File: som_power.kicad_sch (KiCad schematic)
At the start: 94 parts, among them J1 Hermaphroditic_Molex_203456-0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, Q10 DMG1012T-7, Q11 DMG1012T-7, Q17 DMG1012T-7, Q18 DMG1012T-7, Q20 DMG1012T-7, Q22 DMG1012T-7, Q37 DMG1012T-7, Q38 DMG1012T-7, Q7 DMG1012T-7, Q8 DMG1012T-7, SW2 SW_SPDT_PCM12SMTR, U70 MAX16150A_SOT, U72 TPS3840PL30DBVR, U74 SN74LVC2G07DCKR

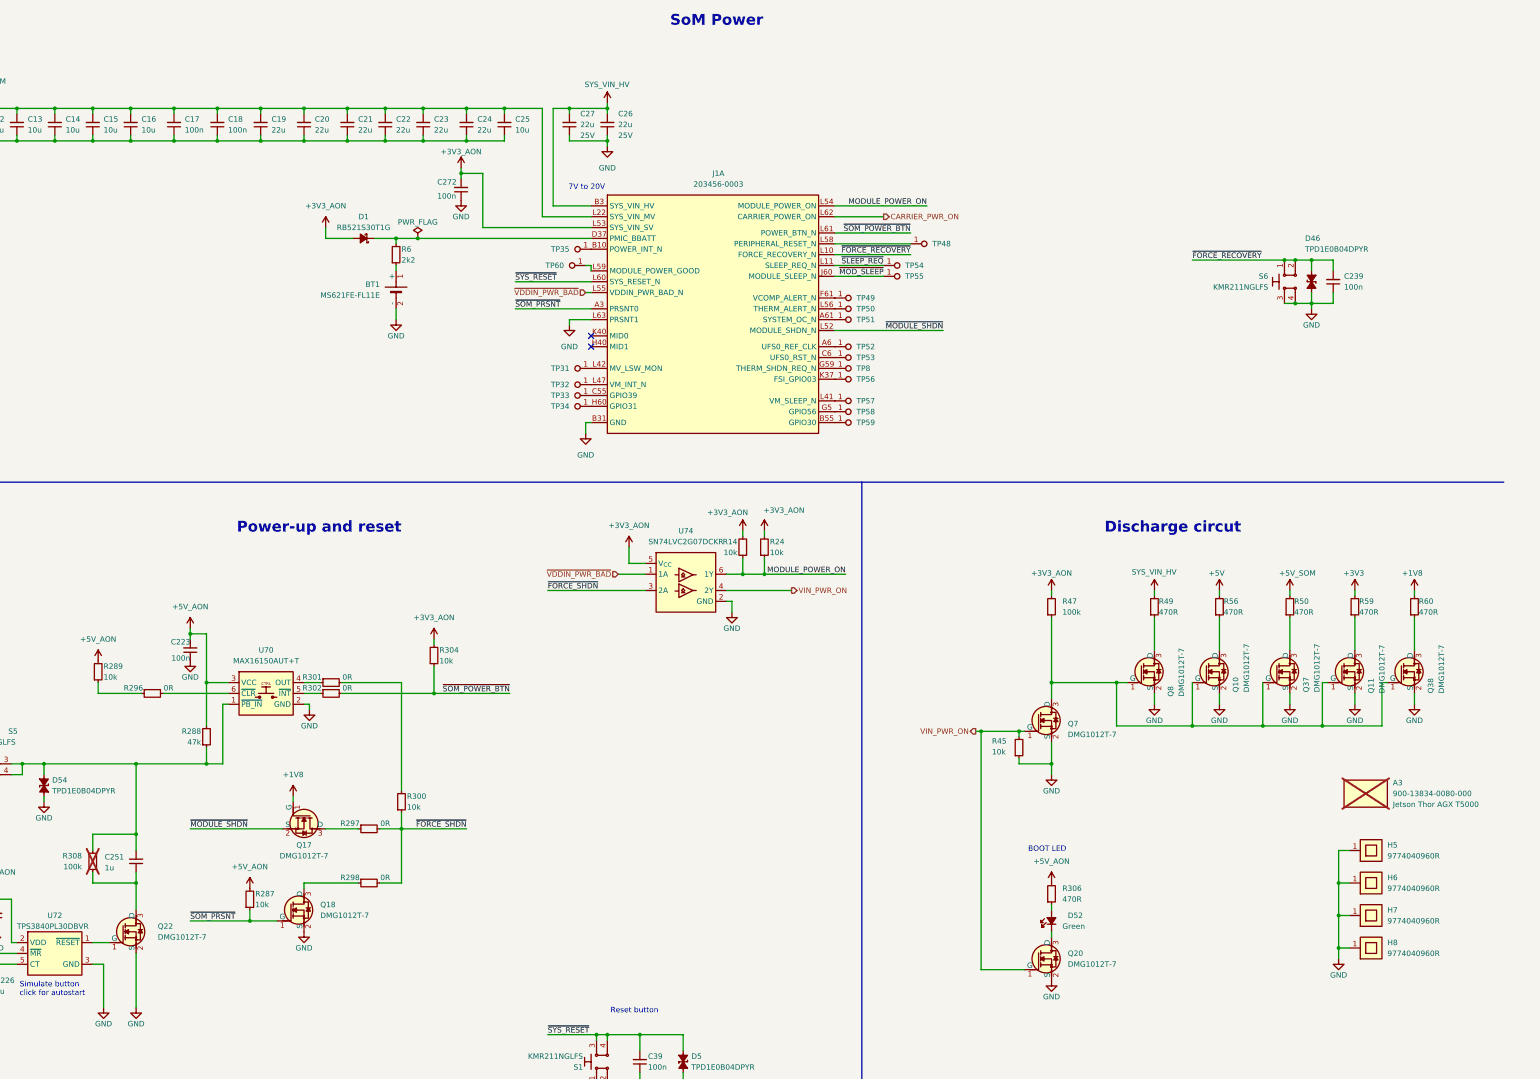
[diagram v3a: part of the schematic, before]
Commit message: [#85488] Update power sequence
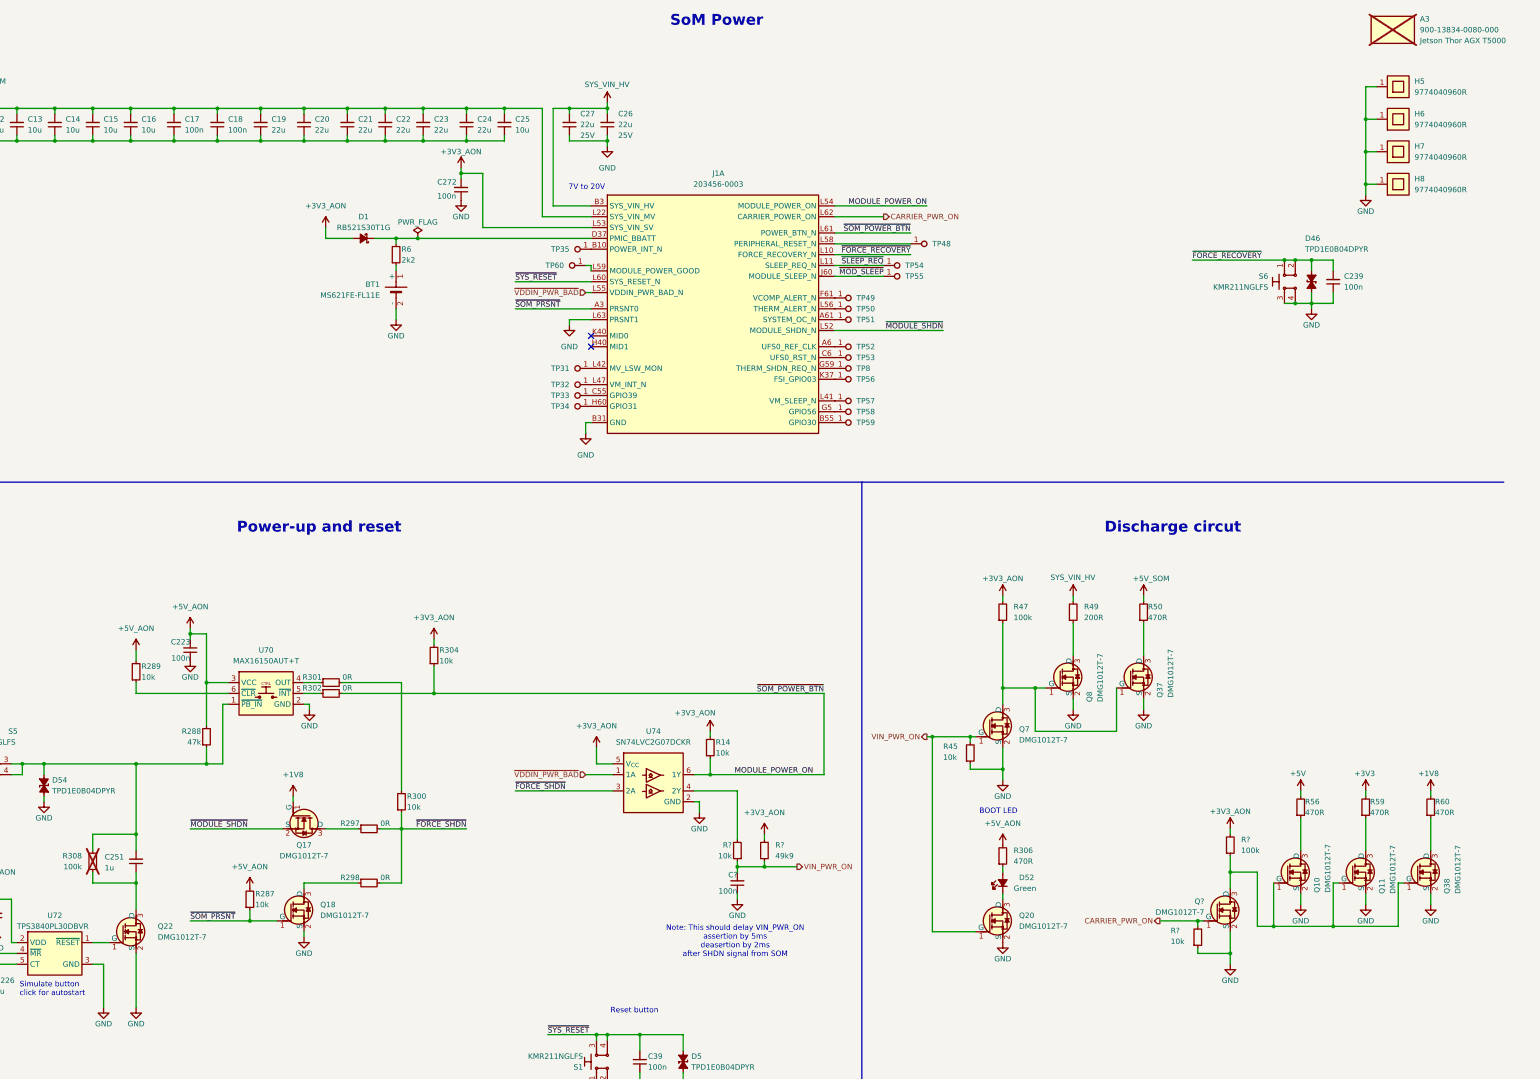
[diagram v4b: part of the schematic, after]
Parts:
- removed R24: R_10k_0402, antmicro-footprints:R_0402_1005Metric, symbol antmicroResistors0402:R_10k_0402
- removed R296: R_0R_0402, antmicro-footprints:R_0402_1005Metric, symbol antmicroResistors0402:R_0R_0402
- added C?: C_100n_0402, antmicro-footprints:C_0402_1005Metric, symbol antmicroCapacitors0402:C_100n_0402
- added Q?: DMG1012T-7, antmicro-footprints:SOT-523, symbol antmicroTransistorsFETsMOSFETsSingle:DMG1012T-7
- added R?: R_100k_0402, antmicro-footprints:R_0402_1005Metric, symbol antmicroResistors0402:R_100k_0402
- added R? (x2): R_10k_0402, antmicro-footprints:R_0402_1005Metric, symbol antmicroResistors0402:R_10k_0402
- added R?: R_100k_0402, antmicro-footprints:R_0402_1005Metric, symbol antmicroResistors0402:R_49k9_0402
- R49: symbol antmicroResistors0402:R_470R_0402 -> antmicroResistors0402:R_200R_0402; MPN CR0402-FX-4700GLF -> CR0402-FX-2000GLF; Val 470R -> 200R
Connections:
- net ~{SOM_POWER_BTN} is gone; now on net MODULE_POWER_ON: J1.L61 (POWER_BTN_N), R302.2, R304.1
- net +3V3_AON: now also R?.2, R?.2
- net CARRIER_PWR_ON: now also Q?.1 (G), R?.2
- net GND: now also C?.1, Q?.2 (S), R?.1
- net VIN_PWR_ON: now also C?.2, R?.1, R?.1; no longer U74.4 (2Y)
- net at Q37.1 (G), Q7.3 (D), Q8.1 (G)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: no longer Q10.1 (G), Q11.1 (G), Q38.1 (G)
- net at R289.1: now also U70.6 (~{CLR})
- new net: Q10.1 (G), Q11.1 (G), Q38.1 (G), Q?.3 (D), R?.1
- new net: R?.2, U74.4 (2Y)
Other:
- note added: "Note: This should delay VIN_PWR_ON assertion by 5ms deasertion by 2ms after SHDN signal from SOM"
- moved on the sheet: A3, D52, H5, H6, H7, H8, Q10, Q11, Q20, Q37, Q38, Q7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

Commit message: [#85488] Annotate sch
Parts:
- gave numbers to parts that had none: 6
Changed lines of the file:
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@@
 	(title_block
 		(title "Jetson AGX Thor Baseboard")
-		(date "2025-10-16")
+		(date "2025-10-21")
 		(rev "1.0.0")
 		(company "Antmicro Ltd")
@@
 		(on_board yes)
 		(dnp no)
-		(property "Reference" "Q?"
+		(property "Reference" "Q40"
 			(at 338.074 227.838 0)
 			(effects
@@
 			(project "jetson-agx-thor-baseboard"
 				(path "/f569b0be-0afd-48b7-93ee-28582a4c645c/33df10a9-5b30-4fa6-b34e-d62ce1b48c65"
-					(reference "Q?")
+					(reference "Q40")
 					(unit 1)
 				)
@@
 		(on_board yes)
 		(dnp no)
-		(property "Reference" "#PWR0760"
+		(property "Reference" "#PWR0768"
 			(at 344.17 214.63 0)
 			(effects
@@
 			(project "jetson-agx-thor-baseboard"
 				(path "/f569b0be-0afd-48b7-93ee-28582a4c645c/33df10a9-5b30-4fa6-b34e-d62ce1b48c65"
-					(reference "#PWR0760")
+					(reference "#PWR0768")
 					(unit 1)
 				)
@@
 		(dnp no)
 		(fields_autoplaced yes)
-		(property "Reference" "R?"
+		(property "Reference" "R363"
 			(at 346.71 213.36 90)
 			(effects
@@
 			(project "jetson-agx-thor-baseboard"
 				(path "/f569b0be-0afd-48b7-93ee-28582a4c645c/33df10a9-5b30-4fa6-b34e-d62ce1b48c65"
-					(reference "R?")
+					(reference "R363")
 					(unit 1)
 				)
@@
 		(on_board yes)
 		(dnp no)
-		(property "Reference" "R?"
+		(property "Reference" "R355"
 			(at 330.2 234.696 90)
 			(effects
@@
 			(project "jetson-agx-thor-baseboard"
 				(path "/f569b0be-0afd-48b7-93ee-28582a4c645c/33df10a9-5b30-4fa6-b34e-d62ce1b48c65"
-					(reference "R?")
+					(reference "R355")
 					(unit 1)
 				)
@@
 		(on_board yes)
 		(dnp no)
-		(property "Reference" "C?"
+		(property "Reference" "C404"
 			(at 228.6 221.615 90)
 			(effects
@@
 			(project "jetson-agx-thor-baseboard"
 				(path "/f569b0be-0afd-48b7-93ee-28582a4c645c/33df10a9-5b30-4fa6-b34e-d62ce1b48c65"
-					(reference "C?")
+					(reference "C404")
 					(unit 1)
 				)
@@
 		(dnp no)
 		(fields_autoplaced yes)
-		(property "Reference" "R?"
+		(property "Reference" "R296"
 			(at 237.49 214.63 90)
 			(effects
@@
 			(project "jetson-agx-thor-baseboard"
 				(path "/f569b0be-0afd-48b7-93ee-28582a4c645c/33df10a9-5b30-4fa6-b34e-d62ce1b48c65"
-					(reference "R?")
+					(reference "R296")
 					(unit 1)
 				)
@@
 		(dnp no)
 		(fields_autoplaced yes)
-		(property "Reference" "#PWR0761"
+		(property "Reference" "#PWR0767"
 			(at 234.95 215.9 0)
 			(effects
@@
 			(project "jetson-agx-thor-baseboard"
 				(path "/f569b0be-0afd-48b7-93ee-28582a4c645c/33df10a9-5b30-4fa6-b34e-d62ce1b48c65"
-					(reference "#PWR0761")
+					(reference "#PWR0767")
 					(unit 1)
 				)
@@
 		(on_board yes)
 		(dnp no)
-		(property "Reference" "R?"
+		(property "Reference" "R24"
 			(at 227.33 214.63 90)
 			(effects
@@
 			(project "jetson-agx-thor-baseboard"
 				(path "/f569b0be-0afd-48b7-93ee-28582a4c645c/33df10a9-5b30-4fa6-b34e-d62ce1b48c65"
-					(reference "R?")
+					(reference "R24")
 					(unit 1)
 				)
@@
 		(on_board yes)
 		(dnp no)
-		(property "Reference" "#PWR0762"
+		(property "Reference" "#PWR0766"
 			(at 237.49 229.87 0)
 			(effects
@@
 			(project "jetson-agx-thor-baseboard"
 				(path "/f569b0be-0afd-48b7-93ee-28582a4c645c/33df10a9-5b30-4fa6-b34e-d62ce1b48c65"
-					(reference "#PWR0762")
+					(reference "#PWR0766")
 					(unit 1)
 				)

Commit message: [#85488] Sch: Fix resistor values
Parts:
- R296: value R_100k_0402 -> R_49k9_0402
- R49: value R_470R_0402 -> R_200R_0402
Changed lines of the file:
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@@
 			)
 		)
-		(property "Value" "R_470R_0402"
+		(property "Value" "R_200R_0402"
 			(at 320.04 142.24 0)
 			(effects
@@
 			)
 		)
-		(property "Value" "R_100k_0402"
+		(property "Value" "R_49k9_0402"
 			(at 247.65 198.12 0)
 			(effects

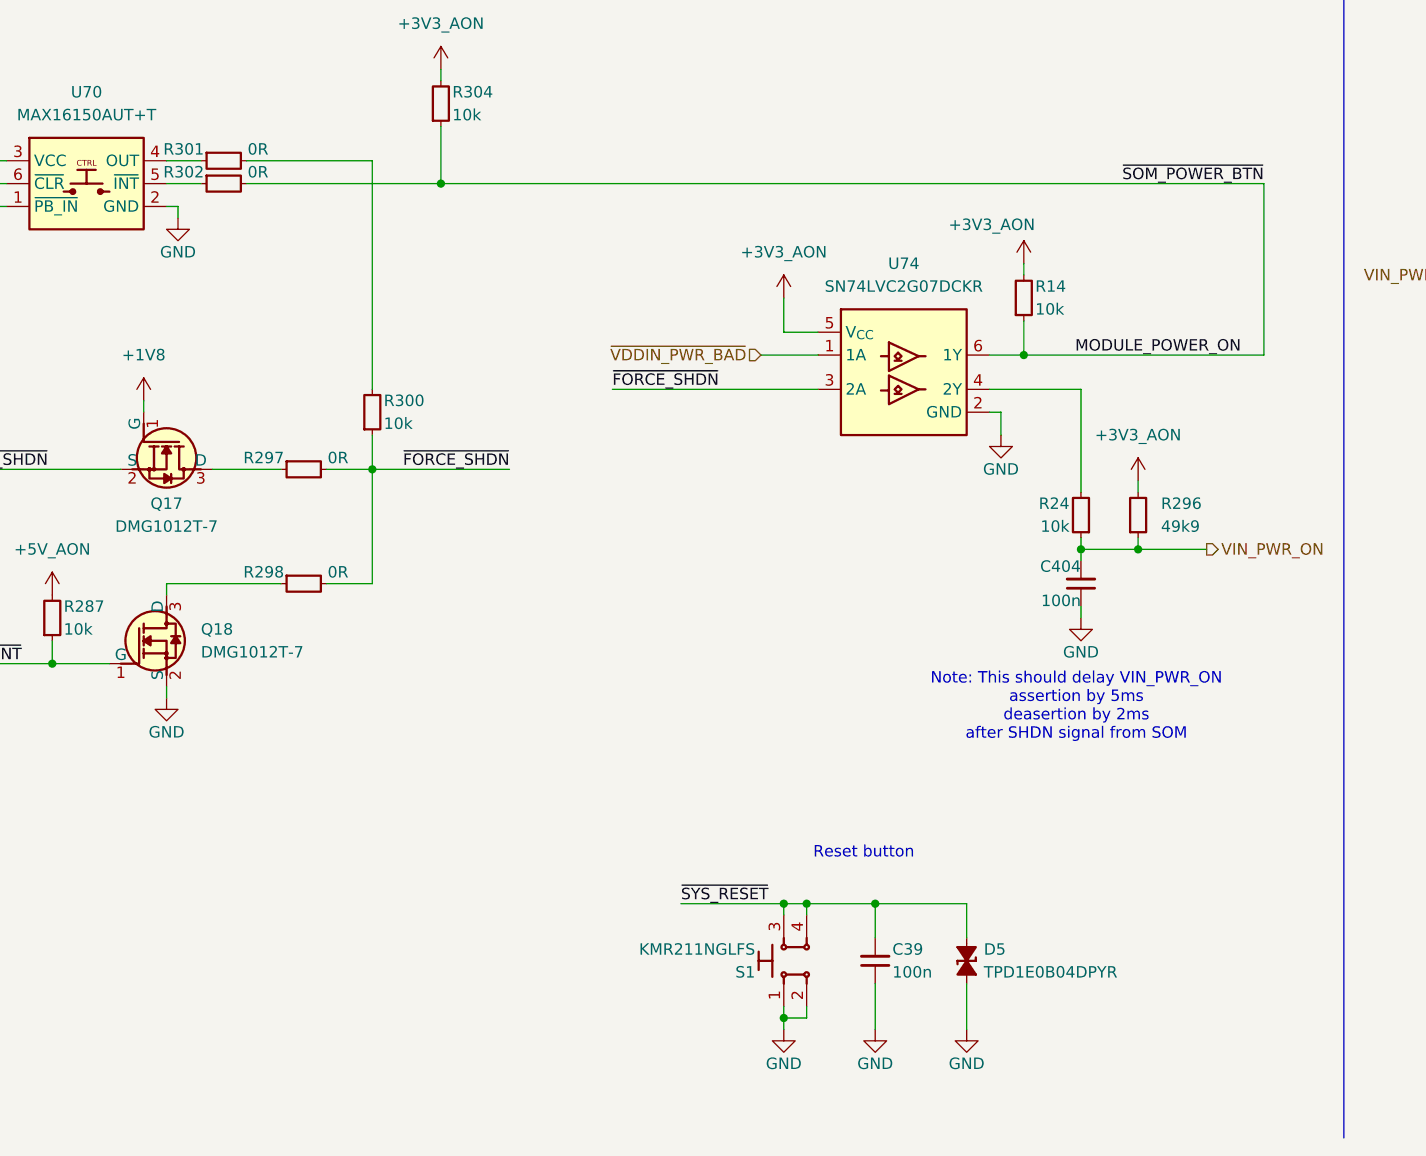
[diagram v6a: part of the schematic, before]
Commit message: [#85326] Update power circuit
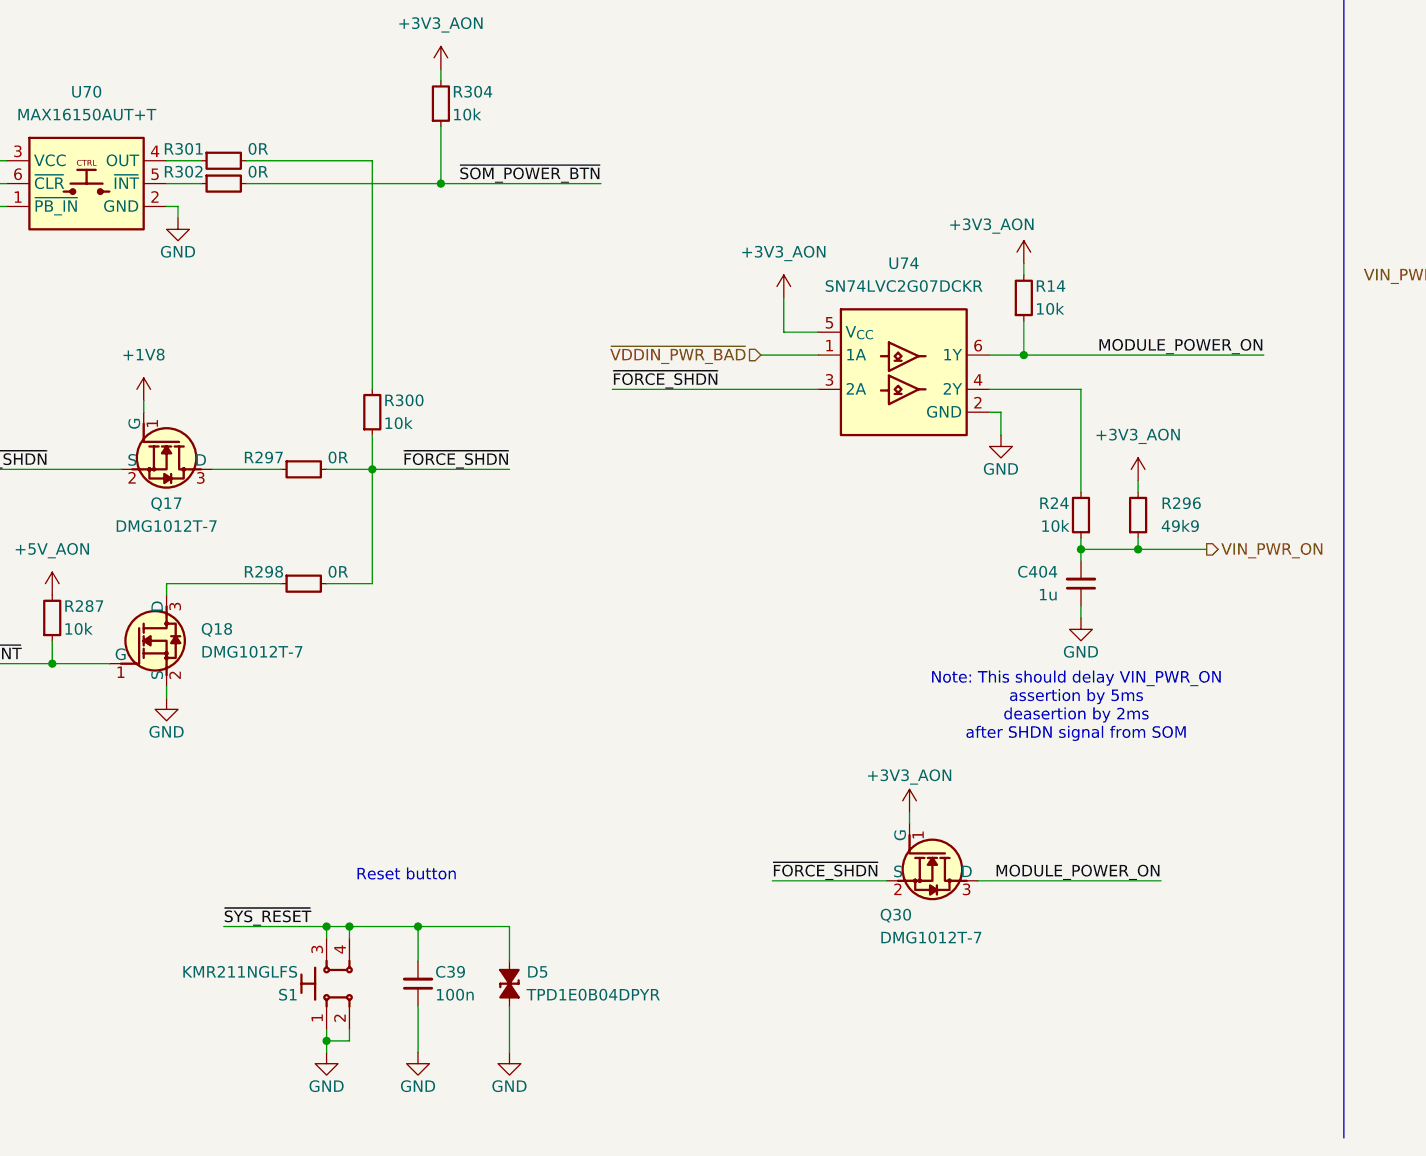
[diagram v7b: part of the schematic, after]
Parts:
- removed C404: C_100n_0402, antmicro-footprints:C_0402_1005Metric, symbol antmicroCapacitors0402:C_100n_0402
- added C404: C_1u_25V_0402, antmicro-footprints:C_0402_1005Metric, symbol antmicroCapacitors0402:C_1u_25V_0402
- added Q30: DMG1012T-7, antmicro-footprints:SOT-523, symbol antmicroTransistorsFETsMOSFETsSingle:DMG1012T-7
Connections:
- net +3V3_AON: now also Q30.1 (G)
- net GND: now also C404.1
- net MODULE_POWER_ON: now also Q30.3 (D); no longer J1.L61 (POWER_BTN_N), R302.2, R304.1
- net VIN_PWR_ON: now also C404.2
- net ~{FORCE_SHDN}: now also Q30.2 (S)
- new net ~{SOM_POWER_BTN}: J1.L61 (POWER_BTN_N), R302.2, R304.1
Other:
- moved on the sheet: C39, D5, S1
